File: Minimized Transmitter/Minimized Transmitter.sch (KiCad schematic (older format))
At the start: 8 parts, among them J1 Conn_ARM_JTAG_SWD_10, J2 Conn_01x02_Male, J3 Conn_01x03_Male, U1 LPC824M201JHI33, U2 RFM69HCW

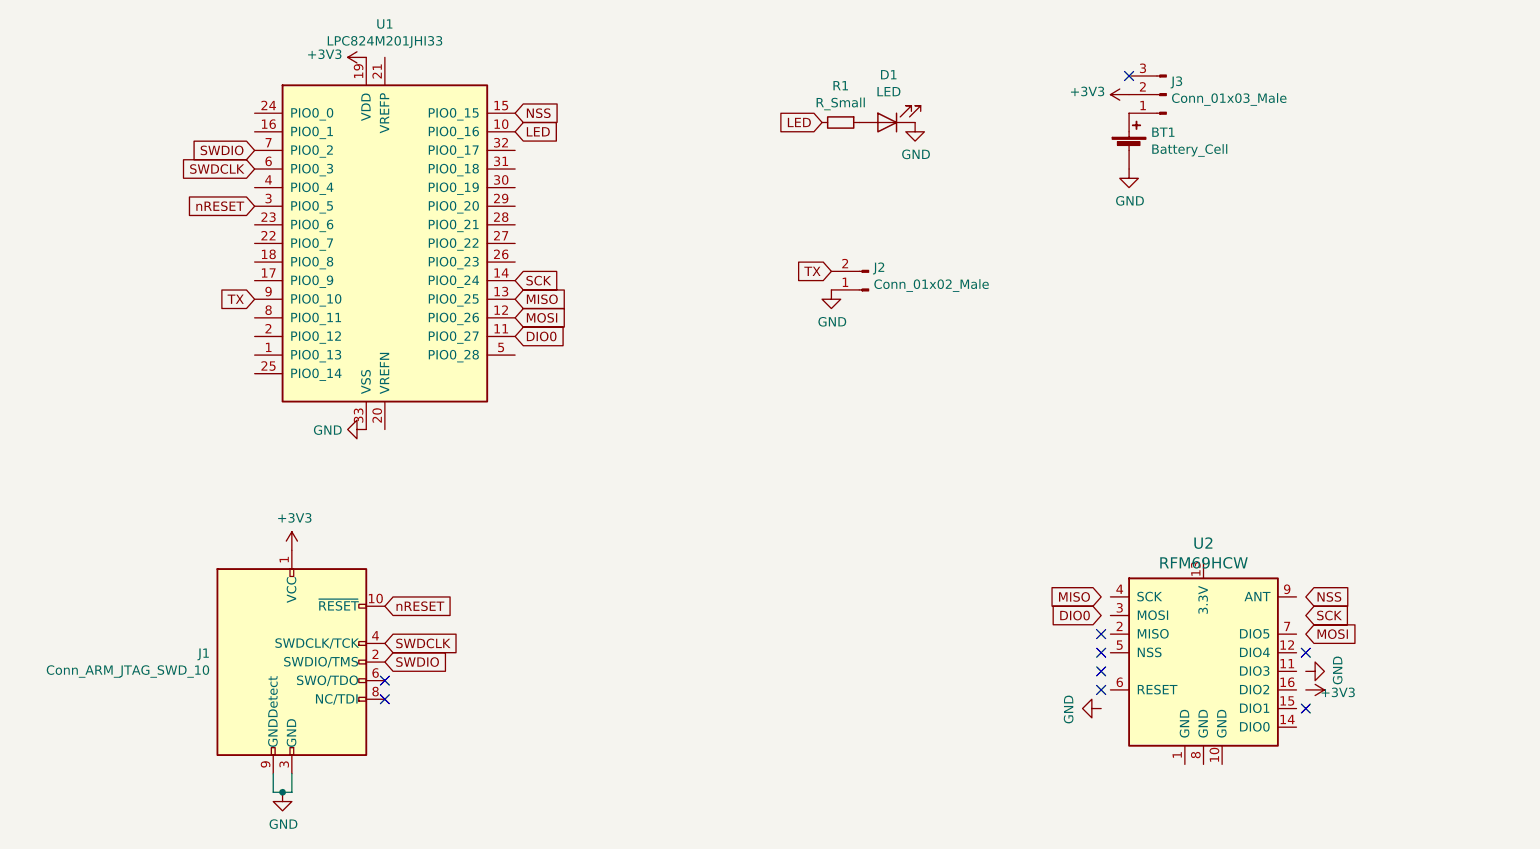
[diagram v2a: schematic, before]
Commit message: Added reset btn and removed on off switch
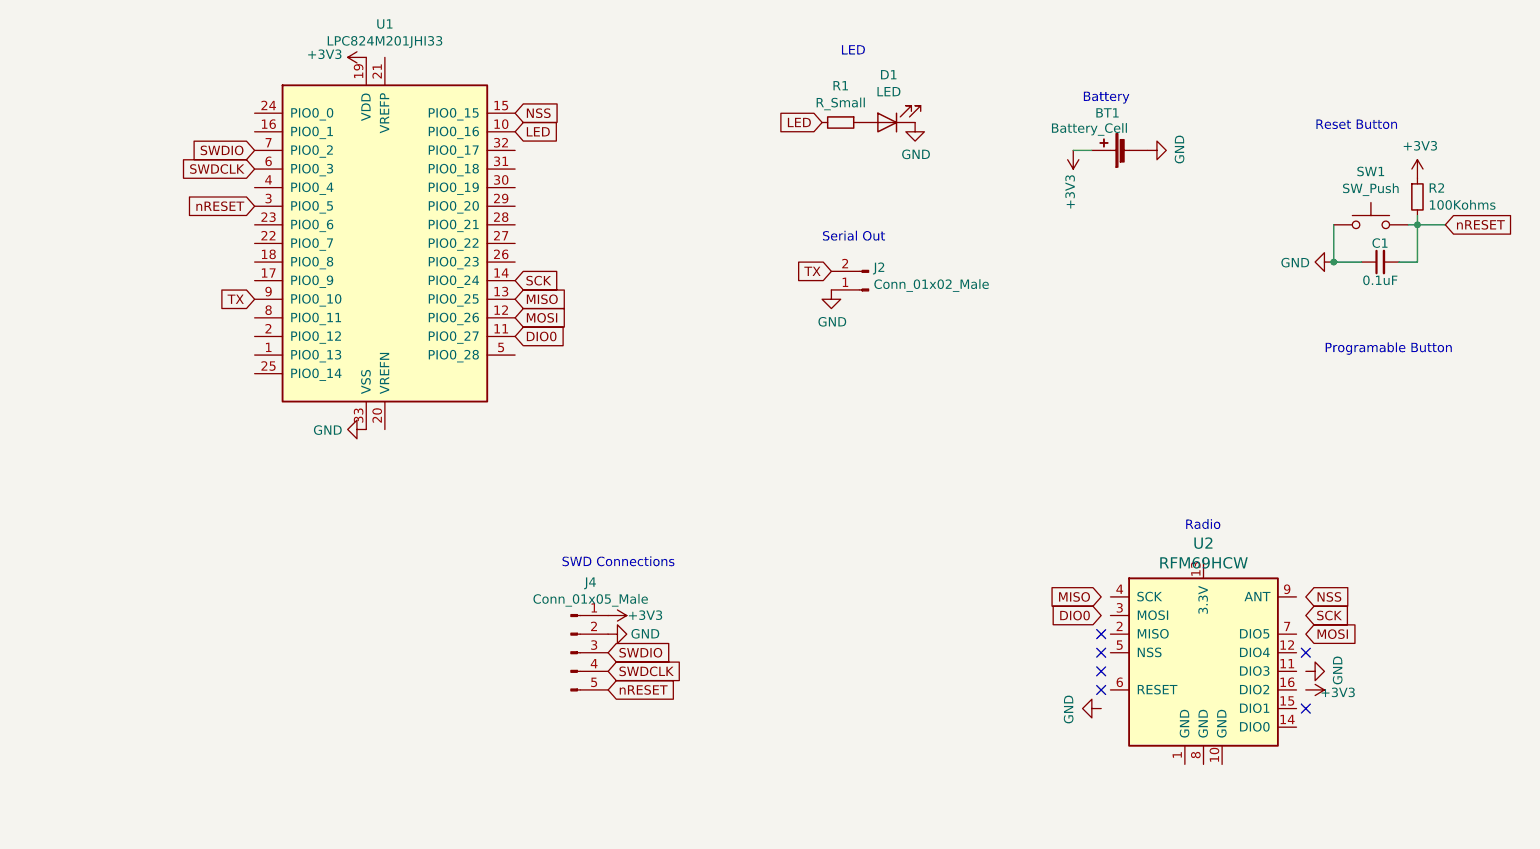
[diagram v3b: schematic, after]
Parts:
- removed J1: Conn_ARM_JTAG_SWD_10, Connector_PinHeader_1.27mm:PinHeader_2x05_P1.27mm_Vertical_SMD, symbol Connector:Conn_ARM_JTAG_SWD_10
- removed J3: Conn_01x03_Male, Connector_PinHeader_2.54mm:PinHeader_1x03_P2.54mm_Vertical, symbol Connector:Conn_01x03_Male
- added C1: 0.1uF, Capacitor_SMD:C_0402_1005Metric, symbol Device:C_Small
- added J4: Conn_01x05_Male, my_foot_prints:SWD_5_Pin_Minimized_SurfaceMount, symbol Connector:Conn_01x05_Male
- added R2: 100Kohms, Resistor_SMD:R_0402_1005Metric, symbol Device:R_Small
- added SW1: SW_Push, my_foot_prints:KMR221GLFS, symbol Switch:SW_Push
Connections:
- net +3V3: now also BT1.1 (+), J4.1 (Pin_1), R2.1
- net GND: now also C1.1, J4.2 (Pin_2), SW1.1
- net SWDCLK: now also J4.4 (Pin_4)
- net SWDIO: now also J4.3 (Pin_3)
- net nRESET: now also C1.2, J4.5 (Pin_5), R2.2, SW1.2
- no-connect marks 9 -> 6
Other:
- note added: "Battery"
- note added: "LED"
- note added: "Programable Button\n"
- note added: "Radio"
- note added: "Reset Button"
- note added: "SWD Connections"
- note added: "Serial Out"
- moved on the sheet: BT1
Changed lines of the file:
@@
-$EndComp
-$Comp
-L Connector:Conn_ARM_JTAG_SWD_10 J1
-U 1 1 5BDB2F11
-P 2000 4550
-F 0 "J1" H 1560 4596 50  0000 R CNN
-F 1 "Conn_ARM_JTAG_SWD_10" H 1560 4505 50  0000 R CNN
-F 2 "Connector_PinHeader_1.27mm:PinHeader_2x05_P1.27mm_Vertical_SMD" H 2050 4000 50  0001 L TNN
-F 3 "http://infocenter.arm.com/help/topic/com.arm.doc.faqs/attached/13634/cortex_debug_connectors.pdf" V 1650 3300 50  0001 C CNN
-	1    2000 4550
-	1    0    0    -1
 $EndComp
 $Comp
@@
 U 1 1 5BDB3AA6
 P 6500 1800
-F 0 "BT1" H 6618 1896 50  0000 L CNN
-F 1 "Battery_Cell" H 6618 1805 50  0000 L CNN
+F 0 "BT1" V 6700 1850 50  0000 L CNN
+F 1 "Battery_Cell" V 6618 1805 50  0000 L CNN
 F 2 "my_foot_prints:PRT-11892" V 6500 1860 50  0001 C CNN
 F 3 "~" V 6500 1860 50  0001 C CNN
 	1    6500 1800
-	1    0    0    -1
+	0    -1   -1   0
 $EndComp
 $Comp
 L power:GND #PWR0105
 U 1 1 5BDB3BBB
-P 6500 1900
-F 0 "#PWR0105" H 6500 1650 50  0001 C CNN
-F 1 "GND" H 6505 1727 50  0000 C CNN
-F 2 "" H 6500 1900 50  0001 C CNN
-F 3 "" H 6500 1900 50  0001 C CNN
-	1    6500 1900
-	1    0    0    -1
-$EndComp
-$Comp
-L power:+3V3 #PWR0106
-U 1 1 5BDB3C26
-P 6500 1500
-F 0 "#PWR0106" H 6500 1350 50  0001 C CNN
-F 1 "+3V3" V 6515 1628 50  0000 L CNN
-F 2 "" H 6500 1500 50  0001 C CNN
-F 3 "" H 6500 1500 50  0001 C CNN
-	1    6500 1500
-	0    -1   -1   0
-$EndComp
-Text GLabel 2500 4550 2    50   Input ~ 0
+P 6600 1800
+F 0 "#PWR0105" H 6600 1550 50  0001 C CNN
+F 1 "GND" H 6605 1627 50  0000 C CNN
+F 2 "" H 6600 1800 50  0001 C CNN
+F 3 "" H 6600 1800 50  0001 C CNN
+	1    6600 1800
+	0    -1   -1   0
+$EndComp
+Text GLabel 3700 4500 2    50   Input ~ 0
 SWDIO
-Text GLabel 2500 4450 2    50   Input ~ 0
+Text GLabel 3700 4600 2    50   Input ~ 0
 SWDCLK
-Text GLabel 2500 4250 2    50   Input ~ 0
+Text GLabel 3700 4700 2    50   Input ~ 0
 nRESET
-NoConn ~ 2500 4650
-NoConn ~ 2500 4750
 $Comp
 L power:GND #PWR0107
 U 1 1 5BDB3CFB
-P 1950 5250
-F 0 "#PWR0107" H 1950 5000 50  0001 C CNN
-F 1 "GND" H 1955 5077 50  0000 C CNN
-F 2 "" H 1950 5250 50  0001 C CNN
-F 3 "" H 1950 5250 50  0001 C CNN
-	1    1950 5250
-	1    0    0    -1
-$EndComp
-Wire Wire Line
-	1950 5250 2000 5250
-Wire Wire Line
-	2000 5250 2000 5150
-Wire Wire Line
-	1950 5250 1900 5250
-Wire Wire Line
-	1900 5250 1900 5150
-Connection ~ 1950 5250
+P 3700 4400
+F 0 "#PWR0107" H 3700 4150 50  0001 C CNN
+F 1 "GND" V 3700 4200 50  0000 C CNN
+F 2 "" H 3700 4400 50  0001 C CNN
+F 3 "" H 3700 4400 50  0001 C CNN
+	1    3700 4400
+	0    -1   -1   0
+$EndComp
 $Comp
 L power:+3V3 #PWR0108
 U 1 1 5BDB3DD2
-P 2000 3950
-F 0 "#PWR0108" H 2000 3800 50  0001 C CNN
-F 1 "+3V3" H 2015 4123 50  0000 C CNN
-F 2 "" H 2000 3950 50  0001 C CNN
-F 3 "" H 2000 3950 50  0001 C CNN
-	1    2000 3950
-	1    0    0    -1
+P 3700 4300
+F 0 "#PWR0108" H 3700 4150 50  0001 C CNN
+F 1 "+3V3" V 3700 4500 50  0000 C CNN
+F 2 "" H 3700 4300 50  0001 C CNN
+F 3 "" H 3700 4300 50  0001 C CNN
+	1    3700 4300
+	0    1    1    0
 $EndComp
 $Comp
@@
 Text GLabel 4850 1650 0    50   Input ~ 0
 LED
-$Comp
-L Connector:Conn_01x03_Male J3
-U 1 1 5BDB404B
-P 6700 1500
-F 0 "J3" H 6673 1430 50  0000 R CNN
-F 1 "Conn_01x03_Male" H 6673 1521 50  0000 R CNN
-F 2 "Connector_PinHeader_2.54mm:PinHeader_1x03_P2.54mm_Vertical" H 6700 1500 50  0001 C CNN
-F 3 "~" H 6700 1500 50  0001 C CNN
-	1    6700 1500
-	-1   0    0    1
-$EndComp
-NoConn ~ 6500 1400
 NoConn ~ 7450 4500
 NoConn ~ 6350 4700
@@
 	0    1    1    0
 $EndComp
+$Comp
+L Connector:Conn_01x05_Male J4
+U 1 1 5C23D507
+P 3500 4500
+F 0 "J4" H 3606 4878 50  0000 C CNN
+F 1 "Conn_01x05_Male" H 3606 4787 50  0000 C CNN
+F 2 "my_foot_prints:SWD_5_Pin_Minimized_SurfaceMount" H 3500 4500 50  0001 C CNN
+F 3 "~" H 3500 4500 50  0001 C CNN
+	1    3500 4500
+	1    0    0    -1
+$EndComp
+$Comp
+L power:+3V3 #PWR0106
+U 1 1 5BDB3C26
+P 6200 1800
+F 0 "#PWR0106" H 6200 1650 50  0001 C CNN
+F 1 "+3V3" V 6215 1928 50  0000 L CNN
+F 2 "" H 6200 1800 50  0001 C CNN
+F 3 "" H 6200 1800 50  0001 C CNN
+	1    6200 1800
+	-1   0    0    1
+$EndComp
+Wire Wire Line
+	6200 1800 6300 1800
+$Comp
+L Switch:SW_Push SW1
+U 1 1 5C23E259
+P 7800 2200
+F 0 "SW1" H 7800 2485 50  0000 C CNN
+F 1 "SW_Push" H 7800 2394 50  0000 C CNN
+F 2 "my_foot_prints:KMR221GLFS" H 7800 2400 50  0001 C CNN
+F 3 "" H 7800 2400 50  0001 C CNN
+	1    7800 2200
+	1    0    0    -1
+$EndComp
+$Comp
+L power:GND #PWR0112
+U 1 1 5C23E2AF
+P 7600 2400
+F 0 "#PWR0112" H 7600 2150 50  0001 C CNN
+F 1 "GND" V 7605 2272 50  0000 R CNN
+F 2 "" H 7600 2400 50  0001 C CNN
+F 3 "" H 7600 2400 50  0001 C CNN
+	1    7600 2400
+	0    1    1    0
+$EndComp
+$Comp
+L power:+3V3 #PWR0113
+U 1 1 5C23E323
+P 8050 1950
+F 0 "#PWR0113" H 8050 1800 50  0001 C CNN
+F 1 "+3V3" H 8065 2123 50  0000 C CNN
+F 2 "" H 8050 1950 50  0001 C CNN
+F 3 "" H 8050 1950 50  0001 C CNN
+	1    8050 1950
+	1    0    0    -1
+$EndComp
+$Comp
+L Device:R_Small R2
+U 1 1 5C23E538
+P 8050 2050
+F 0 "R2" H 8109 2096 50  0000 L CNN
+F 1 "100Kohms" H 8109 2005 50  0000 L CNN
+F 2 "Resistor_SMD:R_0402_1005Metric" H 8050 2050 50  0001 C CNN
+F 3 "~" H 8050 2050 50  0001 C CNN
+	1    8050 2050
+	1    0    0    -1
+$EndComp
+Wire Wire Line
+	8000 2200 8050 2200
+Wire Wire Line
+	8050 2200 8050 2150
+Text GLabel 8200 2200 2    50   Input ~ 0
+nRESET
+Wire Wire Line
+	8200 2200 8050 2200
+Connection ~ 8050 2200
+Wire Wire Line
+	7600 2400 7600 2200
+$Comp
+L Device:C_Small C1
+U 1 1 5C23EB2A
+P 7850 2400
+F 0 "C1" V 7950 2400 50  0000 C CNN
+F 1 "0.1uF" V 7750 2400 50  0000 C CNN
+F 2 "Capacitor_SMD:C_0402_1005Metric" H 7850 2400 50  0001 C CNN
+F 3 "~" H 7850 2400 50  0001 C CNN
+	1    7850 2400
+	0    -1   -1   0
+$EndComp
+Wire Wire Line
+	7750 2400 7600 2400
+Connection ~ 7600 2400
+Wire Wire Line
+	7950 2400 8050 2400
+Wire Wire Line
+	8050 2400 8050 2200
+Text Notes 7500 1700 0    50   ~ 0
+Reset Button
+Text Notes 4850 2300 0    50   ~ 0
+Serial Out
+Text Notes 4950 1300 0    50   ~ 0
+LED
+Text Notes 6250 1550 0    50   ~ 0
+Battery
+Text Notes 6800 3850 0    50   ~ 0
+Radio
+Text Notes 3450 4050 0    50   ~ 0
+SWD Connections
+Text Notes 7550 2900 0    50   ~ 0
+Programable Button\n
 $EndSCHEMATC
